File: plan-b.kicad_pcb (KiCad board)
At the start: 4 copper layers, 18 x 42 mm, 70 parts, among them J1 HRO_TYPE-C-31-M-14, J2 Battery, J3 rgb, J4 columns, J5 Conn_01x10, J6 rows, J7 sensor, J8 Conn_ARM_SWD_TagConnect_TC203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, J9 Conn_01x05_Pin, J99 Net tie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

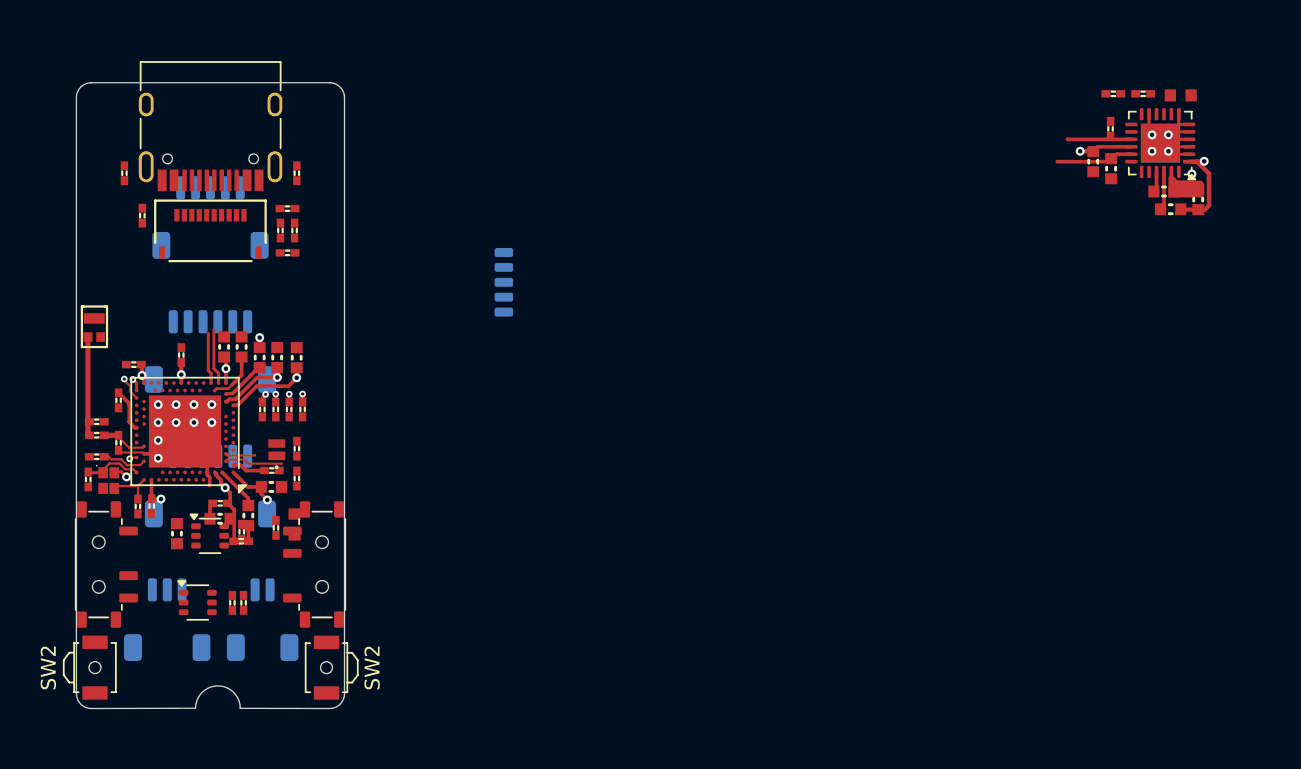
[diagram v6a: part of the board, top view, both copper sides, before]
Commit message: Compacting the right side of the PCB
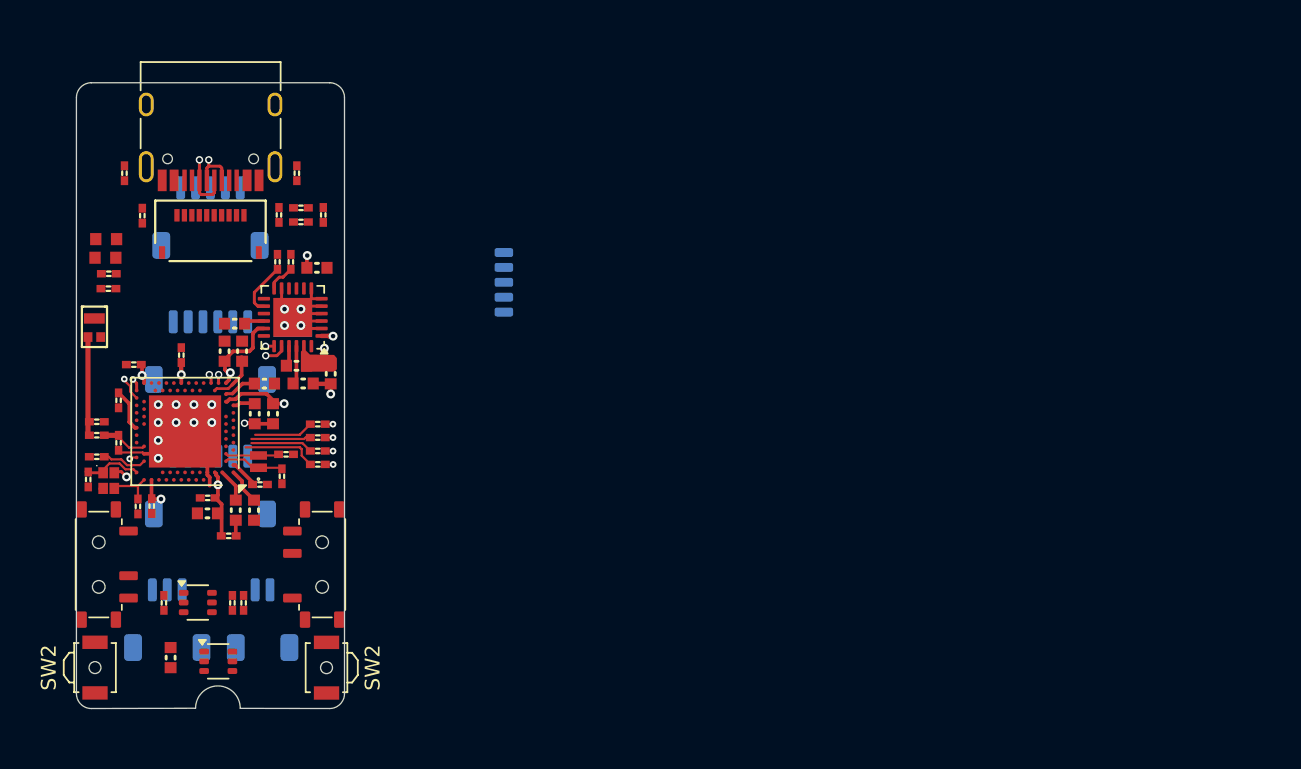
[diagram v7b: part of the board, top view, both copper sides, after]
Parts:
- moved LD2 72.8 mm to (143.0, 68.2), turned to 180 degrees
- moved C22 68.1 mm to (143.2, 71.5), turned to 0 degrees
- moved C25 59.4 mm to (155.8, 76.7)
- moved C26 59.4 mm to (158.1, 77.2)
- moved J99 59.4 mm to (157.7, 75.9)
- moved L5 59.4 mm to (156.2, 77.8)
- moved U2 59.4 mm to (155.5, 73.4)
- moved C23 58.7 mm to (151.6, 73.8), turned to 0 degrees
- moved R_ICHG1 58.3 mm to (155.4, 69.7), turned to -90 degrees
- moved R3 57.2 mm to (154.5, 69.7), turned to 90 degrees
- moved C24 53.7 mm to (157.2, 70.1), turned to 180 degrees
- moved LD3 22.0 mm to (142.9, 69.4), turned to 180 degrees
- moved R_BLE1 20.4 mm to (143.2, 70.5), turned to 180 degrees
- moved U4 8.44 mm to (150.5, 96.5)
- moved C44 8.34 mm to (147.3, 96.2)
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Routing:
- net VDD: track 15.1 -> 9.55 mm, vias 6 -> 3
- net Sensor CS: track 0.00 -> 5.09 mm
- net VBAT: track 4.30 -> 0.00 mm
- net Sensor SDIO: track 0.00 -> 4.17 mm
- net Sensor IRQ: track 0.00 -> 4.00 mm
- net Sensor CLK: track 0.00 -> 4.00 mm
- net 1.8v: track 6.38 -> 2.70 mm, vias 1 -> 2
- net Net-(U2-NTC): track 0.00 -> 3.63 mm
- net D+: track 3.41 -> 6.47 mm, vias 0 -> 3
- net VSYS: track 8.34 -> 5.95 mm, vias 2 -> 1
- net Net-(U2-ICHG): track 0.00 -> 1.90 mm
- net Net-(U1-P0.01/XL2): track 2.00 -> 3.61 mm
- net D-: track 3.69 -> 4.51 mm, vias 0 -> 3
- net GND: track 21.4 -> 22.2 mm, vias 16 -> 17
- net Net-(U1-DEC4): track 5.60 -> 4.83 mm
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
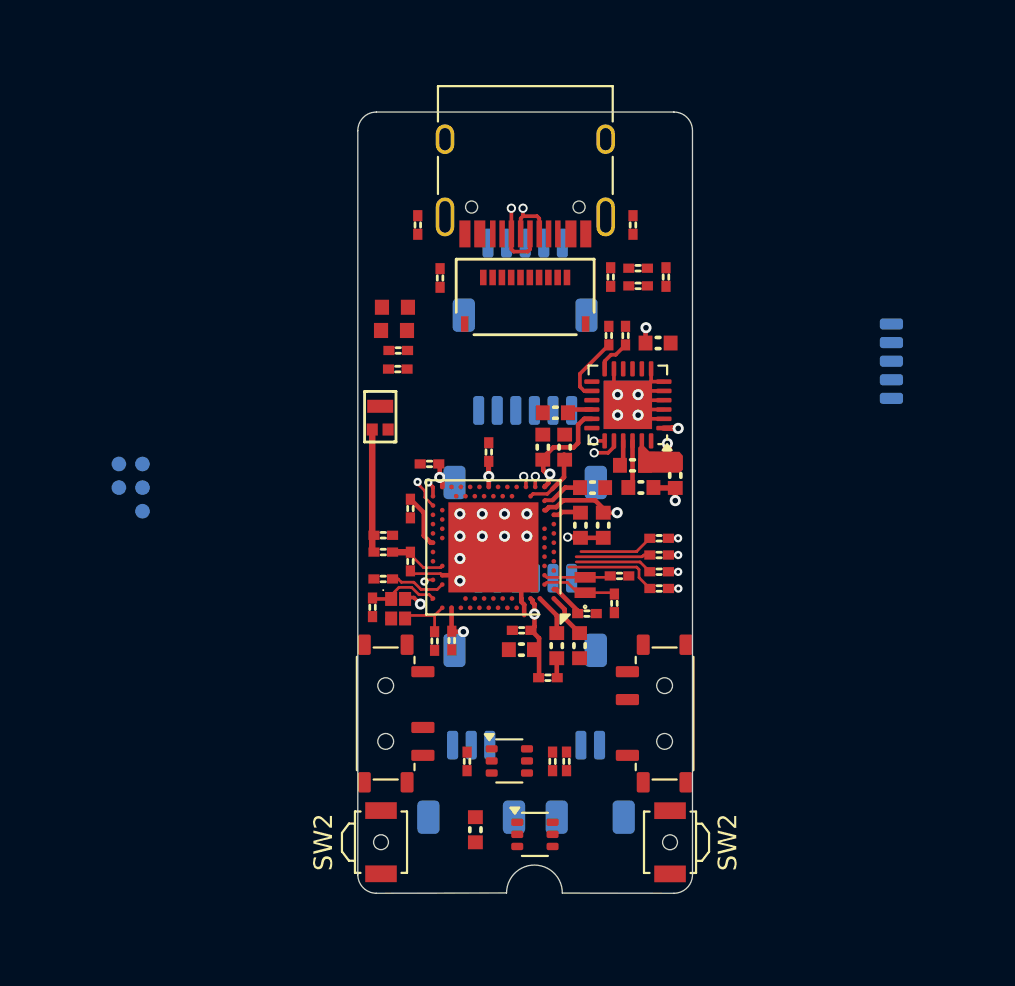
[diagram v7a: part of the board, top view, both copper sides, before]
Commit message: Reworking the PSU block and squeeshing everything into 16x42mm space
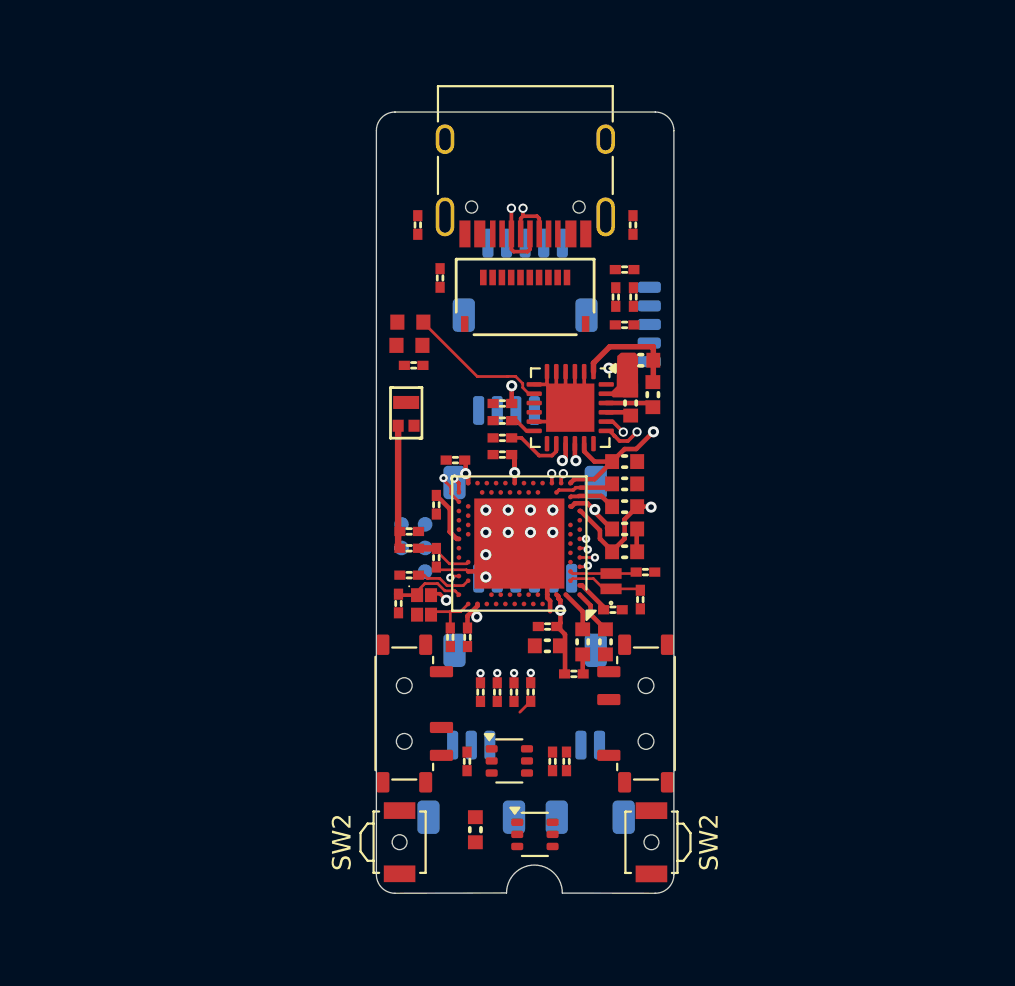
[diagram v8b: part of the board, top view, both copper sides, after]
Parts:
- removed C23: 10µF, Library:C_0603_1608
- removed C24: 2.2µF, Library:C_0603_1608
- moved J8 15.5 mm to (144.0, 81.1)
- moved J9 13.2 mm to (158.3, 69.1)
- moved R16 12.7 mm to (147.6, 88.8), turned to 90 degrees
- moved R15 11.4 mm to (148.5, 88.8), turned to 90 degrees
- moved R14 10.1 mm to (149.4, 88.8), turned to 90 degrees
- moved R11 8.88 mm to (150.3, 88.8), turned to 90 degrees
- moved R_ICHG1 8.05 mm to (148.8, 74.2), turned to 0 degrees
- moved R3 7.94 mm to (148.8, 75.2), turned to 180 degrees
- moved C26 6.47 mm to (156.2, 71.0), turned to 0 degrees
- moved C22 5.92 mm to (148.8, 73.3)
- moved J99 5.23 mm to (154.9, 71.4), turned to 0 degrees
- moved L5 5.03 mm to (156.9, 72.8), turned to -90 degrees
- moved C21 4.47 mm to (155.3, 76.5), turned to 0 degrees
- moved C20 3.78 mm to (155.3, 77.7), turned to 0 degrees
- moved C30 3.40 mm to (155.3, 69.1), turned to 0 degrees
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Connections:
- net LCD CLK renamed CLK
- net LCD CS renamed CS
- net LCD DATA renamed DATA
- AE1 pad 2: GND -> (no net)
- U1 pad G1: unconnected-(U1-P0.26-PadG1) -> Sensor CS
- U1 pad J1: unconnected-(U1-P0.04/AIN2-PadJ1) -> Sensor SDIO
- U1 pad L1: unconnected-(U1-P0.06-PadL1) -> Sensor CLK
- U1 pad N1: unconnected-(U1-P0.08-PadN1) -> Sensor IRQ
- X1 pad 2: GND -> unconnected-(X1-GND-Pad2)
- X1 pad 4: GND -> unconnected-(X1-GND-Pad4)
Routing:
- net Net-(LD2-C): track 0.00 -> 7.70 mm
- net VDD: track 9.55 -> 14.5 mm, vias 3 -> 4
- net Sensor CS: track 5.09 -> 1.29 mm, vias 0 -> 1
- net Sensor IRQ: track 4.00 -> 0.34 mm, vias 0 -> 1
- net Sensor CLK: track 4.00 -> 0.46 mm, vias 0 -> 1
- net Sensor SDIO: track 4.17 -> 0.82 mm, vias 0 -> 1
- net 1.8v: track 2.70 -> 6.01 mm, vias 2 -> 0
- net GND: track 22.2 -> 20.3 mm, vias 17 -> 11
- net VBAT: track 0.00 -> 1.93 mm, vias 0 -> 2
- net VSYS: track 5.95 -> 4.17 mm, vias 1 -> 2
- net D-: track 4.51 -> 5.99 mm
- net unconnected-(X1-GND-Pad4): track 0.00 -> 1.17 mm, vias 0 -> 1
- net D+: track 6.47 -> 5.81 mm
- net VBUS: track 7.20 -> 7.75 mm, vias 2 -> 1
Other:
- board size 18 x 42 mm -> 16 x 42 mm
